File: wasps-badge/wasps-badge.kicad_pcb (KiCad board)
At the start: 2 copper layers, 75 x 75 mm, 24 parts, among them J1 Conn_Debug, J2 Conn_AddOn, J3 Conn_CTF, SW1 SW_SPDT, SW2 SW_Push, SW3 SW_Push, U1 CH32V003FxPx

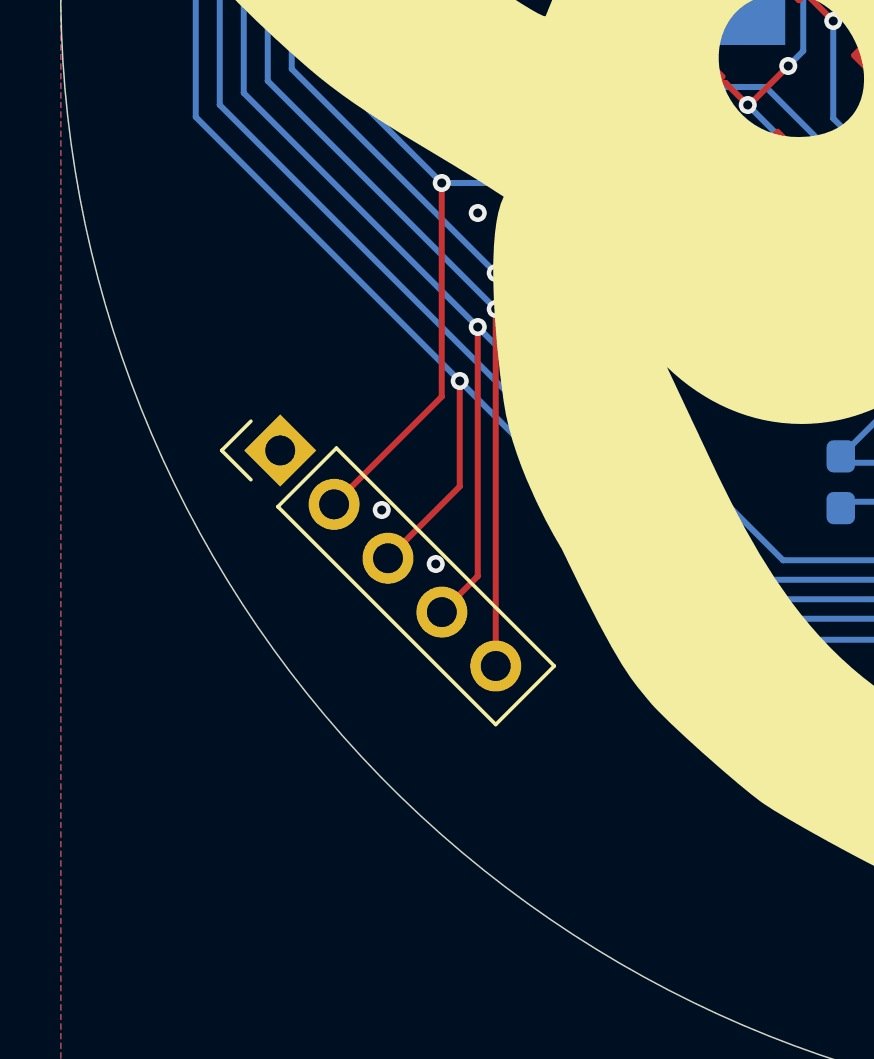
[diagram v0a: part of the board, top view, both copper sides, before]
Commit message: Fix CTF header position
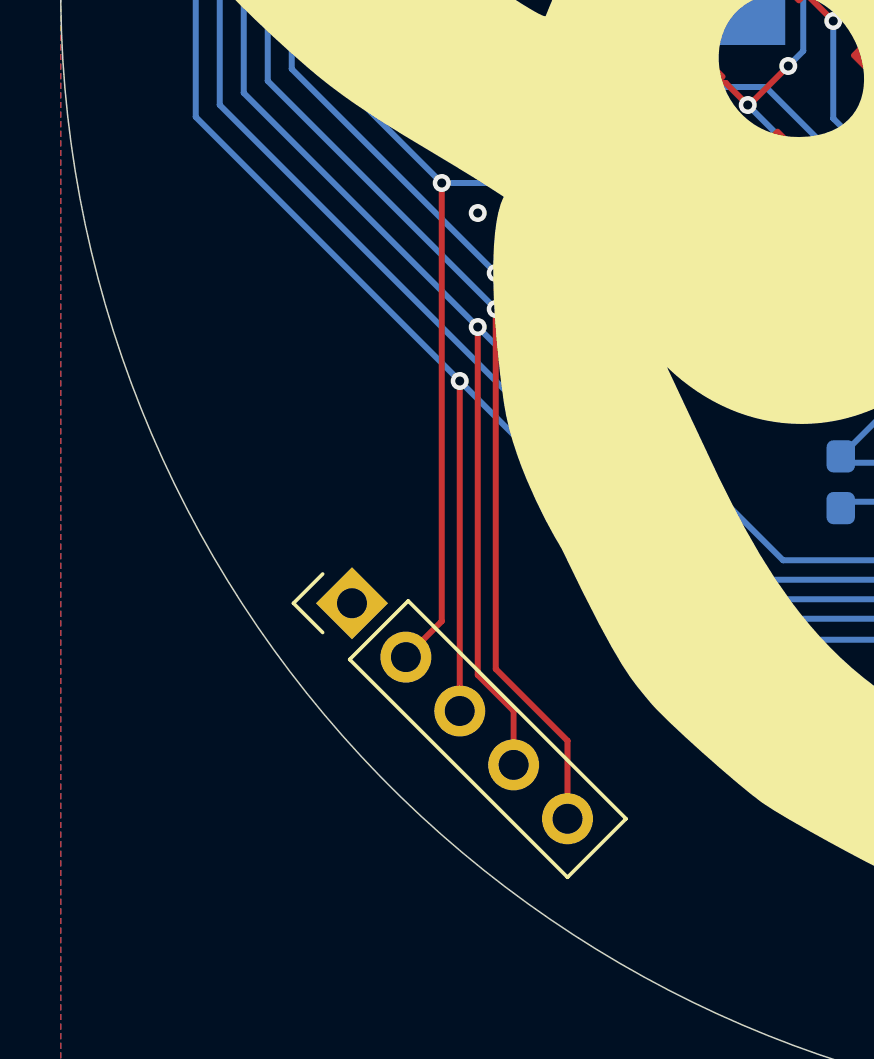
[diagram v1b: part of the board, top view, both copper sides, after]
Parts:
- moved J3 5.63 mm to (72.2, 120.4)
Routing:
- net /CTF_4: track 78.8 -> 84.9 mm
- net /CTF_3: track 79.4 -> 84.5 mm
- net /CTF_I: track 68.1 -> 72.2 mm
- net /CTF_1: track 70.6 -> 74.7 mm
- net GND: vias 4 -> 2
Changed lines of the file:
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@@
 	(footprint "Connector_PinHeader_2.54mm:PinHeader_1x05_P2.54mm_Vertical"
 		(layer "F.Cu")
-		(at 69.815795 115.315795 45)
+		(at 72.207898 120.407898 45)
 		(descr "Through hole straight pin header, 1x05, 2.54mm pitch, single row")
 		(tags "Through hole pin header THT 1x05 2.54mm single row")
@@
 	)
 	(via
-		(at 73.2 117.3)
-		(size 0.6)
-		(drill 0.3)
-		(layers "F.Cu" "B.Cu")
-		(free yes)
-		(net 1)
-	)
-	(via
-		(at 75 119.1)
-		(size 0.6)
-		(drill 0.3)
-		(layers "F.Cu" "B.Cu")
-		(free yes)
-		(net 1)
-	)
-	(via
 		(at 107.25 104.5)
 		(size 0.6)
@@
 	)
 	(segment
-		(start 75.2 113.523692)
-		(end 75.2 106.4)
+		(start 75.2 106.4)
+		(end 75.2 121.007898)
 		(width 0.2)
 		(layer "F.Cu")
@@
 	)
 	(segment
-		(start 71.611846 117.111846)
-		(end 75.2 113.523692)
+		(start 75.2 121.007898)
+		(end 74.003949 122.203949)
 		(width 0.2)
 		(layer "F.Cu")
@@
 	)
 	(segment
-		(start 77 122.5)
-		(end 77 110.6)
+		(start 77 110.6)
+		(end 77 122.6)
+		(width 0.2)
+		(layer "F.Cu")
+		(net 14)
+	)
+	(segment
+		(start 77 122.6)
+		(end 79.392103 124.992103)
+		(width 0.2)
+		(layer "F.Cu")
+		(net 14)
+	)
+	(segment
+		(start 79.392103 124.992103)
+		(end 79.392103 127.592103)
 		(width 0.2)
 		(layer "F.Cu")
@@
 	)
 	(segment
-		(start 76.4 119.507898)
-		(end 76.4 111.2)
+		(start 76.4 122.8)
+		(end 77.596052 123.996052)
 		(width 0.2)
 		(layer "F.Cu")
@@
 	)
 	(segment
-		(start 75.203949 120.703949)
-		(end 76.4 119.507898)
+		(start 77.596052 123.996052)
+		(end 77.596052 125.796052)
+		(width 0.2)
+		(layer "F.Cu")
+		(net 15)
+	)
+	(segment
+		(start 76.4 111.2)
+		(end 76.4 122.8)
 		(width 0.2)
 		(layer "F.Cu")
@@
 	)
 	(segment
-		(start 73.407897 118.907897)
-		(end 75.8 116.515794)
-		(width 0.2)
-		(layer "F.Cu")
-		(net 16)
-	)
-	(segment
-		(start 75.8 116.515794)
-		(end 75.8 113)
+		(start 75.8 113)
+		(end 75.8 124)
 		(width 0.2)
 		(layer "F.Cu")

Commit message: Add labeling
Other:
- board text added: "${TITLE} Rev. ${REVISION} ${URL}"
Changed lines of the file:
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@@
 	)
 	(paper "A4")
+	(title_block
+		(title "${TITLE}")
+		(date "${DATE}")
+		(rev "${REVISION}")
+		(company "${COMPANY}")
+	)
 	(layers
 		(0 "F.Cu" signal)
@@
 		)
 	)
+	(property "COMPANY" "Wicked Agile Stinging Pests Society")
+	(property "DATE" "2025-12-15")
+	(property "GITHUB_PREFIX" "github.com/lizardperson42/")
+	(property "GITHUB_PROJECT" "wasps-badge")
+	(property "REVISION" "1")
+	(property "TITLE" "WASPS Badge")
+	(property "URL" "https://wasp.systems")
 	(net 0 "")
 	(net 1 "GND")
@@
 		)
 	)
+	(gr_text "${TITLE}\nRev. ${REVISION}\n${URL}"
+		(at 100.5 127.5 0)
+		(layer "B.SilkS")
+		(effects
+			(font
+				(size 1 1)
+				(thickness 0.125)
+			)
+			(justify mirror)
+		)
+	)

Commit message: Add more vias
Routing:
- net /NRST: track 103.3 -> 102.7 mm
- net GND: vias 2 -> 40
